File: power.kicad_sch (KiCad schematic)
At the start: 19 parts, among them IC1 RT8096AHGJ5, IC2 TLV61070A, Q1 SSM3J35AMFV

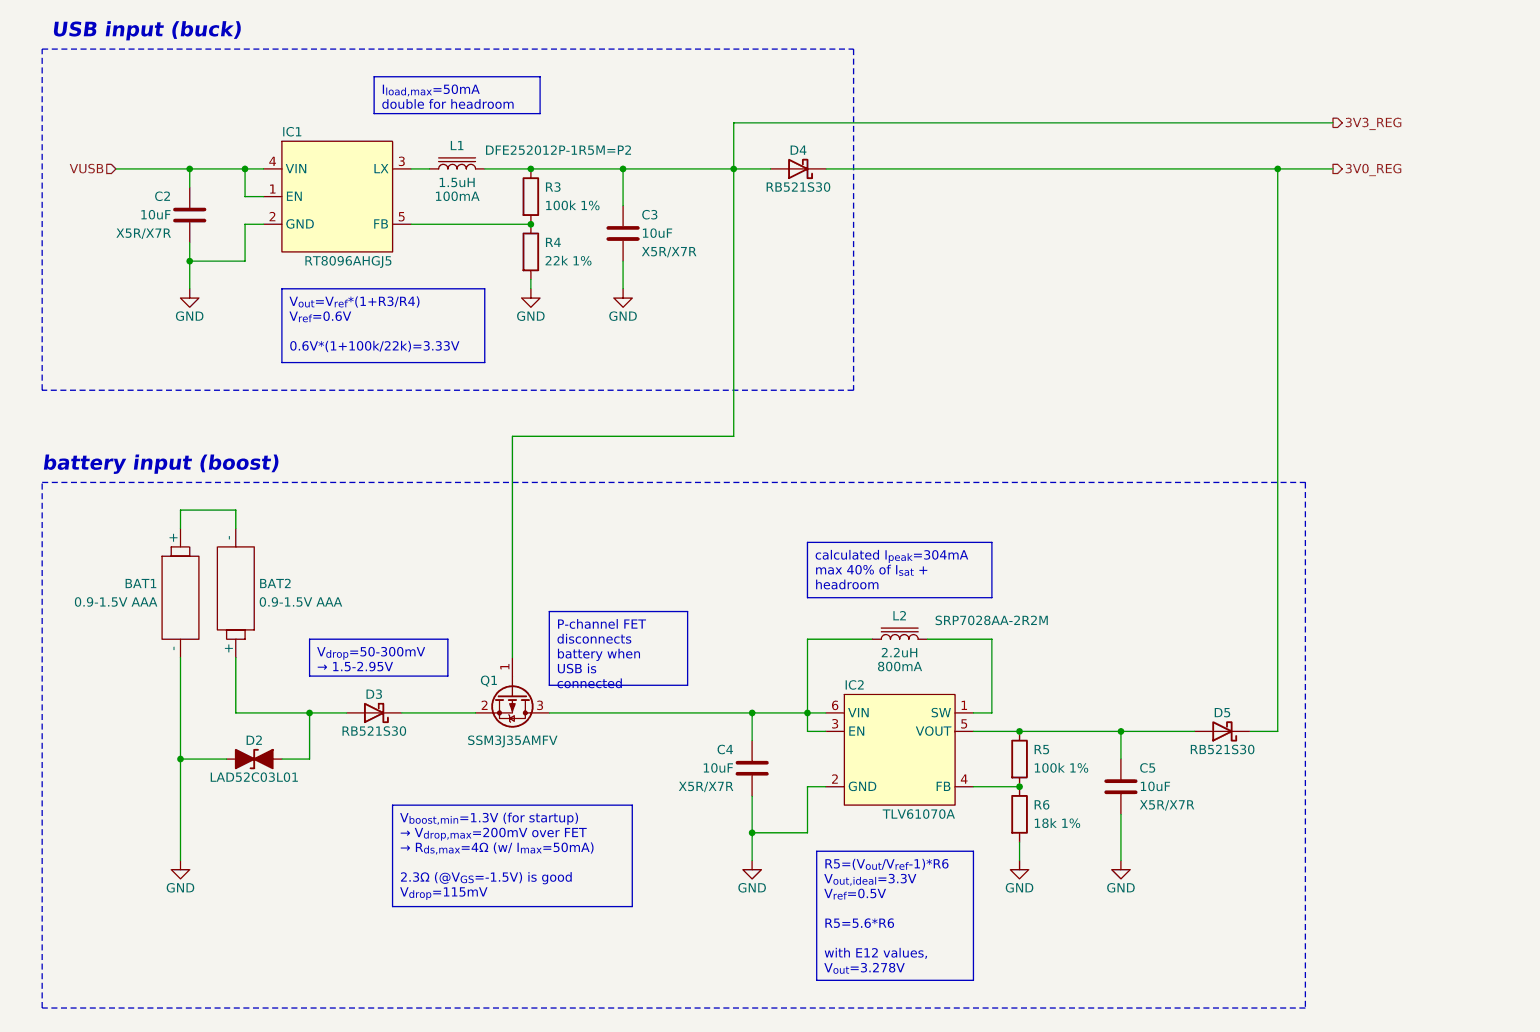
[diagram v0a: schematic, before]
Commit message: added testpoints
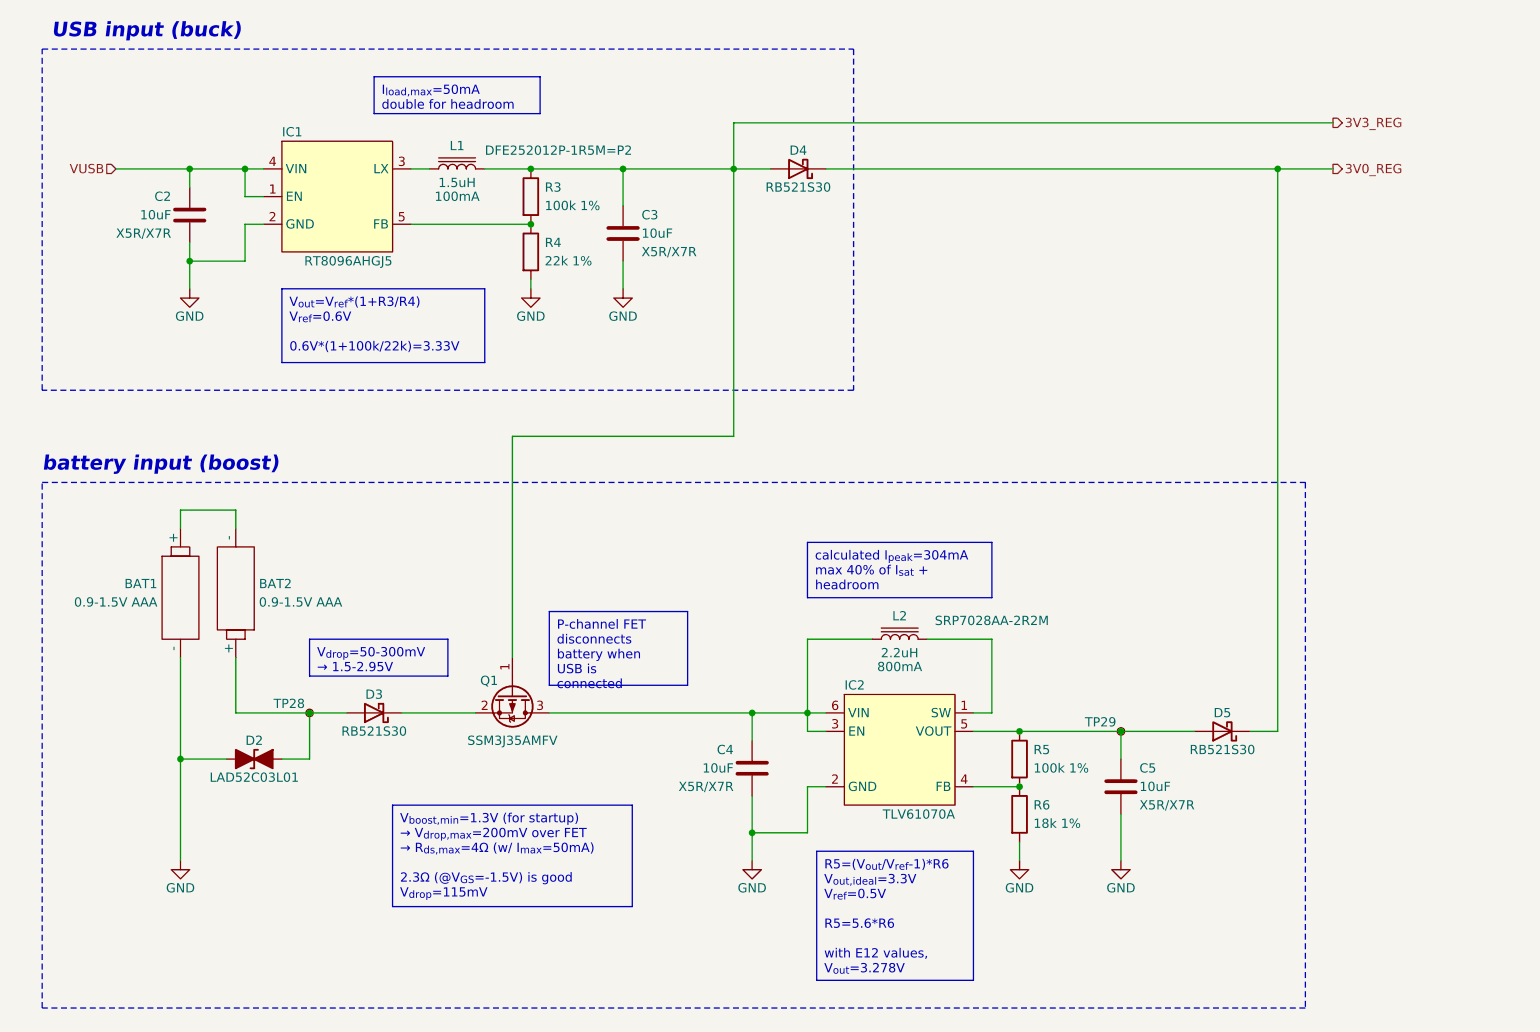
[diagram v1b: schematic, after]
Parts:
- added TP28, TP29: TestPoint_Small, TestPoint:TestPoint_Pad_D2.0mm, symbol Connector:TestPoint_Small
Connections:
- net at C5.1, D5.2 (A), IC2.5 (VOUT)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: now also TP29.1
- net at BAT2.1 (+), D2.2 (A2), D3.2 (A): now also TP28.1
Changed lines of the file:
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@@
     (stroke (width 0) (type default))
   )
-  (wire (pts (xy 233.68 41.91) (xy 151.13 41.91))
+  (wire (pts (xy 151.13 41.91) (xy 233.68 41.91))
     (stroke (width 0) (type default))
   )
@@
     (stroke (width 0) (type default))
   )
+  (wire (pts (xy 163.83 48.26) (xy 226.06 48.26))
+    (stroke (width 0) (type default))
+  )
   (wire (pts (xy 222.25 125.73) (xy 226.06 125.73))
     (stroke (width 0) (type default))
@@
   )
   (wire (pts (xy 161.29 113.03) (xy 161.29 123.19))
-    (stroke (width 0) (type default))
-  )
-  (wire (pts (xy 163.83 48.26) (xy 226.06 48.26))
     (stroke (width 0) (type default))
   )
@@
     )
   )
+  (symbol (lib_id "Connector:TestPoint_Small") (at 92.71 123.19 0) (mirror y) (unit 1)
+    (in_bom yes) (on_board yes) (dnp no)
+    (property "Reference" "TP28" (at 92.075 121.92 0)
+      (effects (font (size 1.27 1.27)) (justify left))
+    )
+    (property "Value" "TestPoint_Small" (at 91.44 124.46 0)
+      (effects (font (size 1.27 1.27)) (justify left) hide)
+    )
+    (property "Footprint" "TestPoint:TestPoint_Pad_D2.0mm" (at 87.63 123.19 0)
+      (effects (font (size 1.27 1.27)) hide)
+    )
+    (property "Datasheet" "~" (at 87.63 123.19 0)
+      (effects (font (size 1.27 1.27)) hide)
+    )
+    (pin "1")
+    (instances
+      (project "gkos_pebble"
+        (path "/ab6fff6e-44fa-4992-ab9d-8d9a7df4367d/cd56f630-7868-414d-908b-81d1bc89adae"
+          (reference "TP28") (unit 1)
+        )
+      )
+    )
+  )
   (symbol (lib_id "Device:R") (at 190.5 137.16 0) (unit 1)
     (in_bom yes) (on_board yes) (dnp no)
@@
   (symbol (lib_id "power:GND") (at 76.2 64.77 0) (unit 1)
     (in_bom yes) (on_board yes) (dnp no)
-    (property "Reference" "#PWR09" (at 76.2 71.12 0)
+    (property "Reference" "#PWR010" (at 76.2 71.12 0)
       (effects (font (size 1.27 1.27)) hide)
     )
@@
       (project "gkos_pebble"
         (path "/ab6fff6e-44fa-4992-ab9d-8d9a7df4367d/cd56f630-7868-414d-908b-81d1bc89adae"
-          (reference "#PWR09") (unit 1)
+          (reference "#PWR010") (unit 1)
         )
       )
@@
   (symbol (lib_id "power:GND") (at 74.93 143.51 0) (unit 1)
     (in_bom yes) (on_board yes) (dnp no)
-    (property "Reference" "#PWR010" (at 74.93 149.86 0)
+    (property "Reference" "#PWR09" (at 74.93 149.86 0)
       (effects (font (size 1.27 1.27)) hide)
     )
@@
       (project "gkos_pebble"
         (path "/ab6fff6e-44fa-4992-ab9d-8d9a7df4367d/cd56f630-7868-414d-908b-81d1bc89adae"
-          (reference "#PWR010") (unit 1)
+          (reference "#PWR09") (unit 1)
         )
       )
@@
         )
       )
+    )
+  )
+  (symbol (lib_id "Connector:TestPoint_Small") (at 204.47 125.73 0) (mirror y) (unit 1)
+    (in_bom yes) (on_board yes) (dnp no)
+    (property "Reference" "TP29" (at 203.835 124.46 0)
+      (effects (font (size 1.27 1.27)) (justify left))
+    )
+    (property "Value" "TestPoint_Small" (at 203.2 127 0)
+      (effects (font (size 1.27 1.27)) (justify left) hide)
+    )
+    (property "Footprint" "TestPoint:TestPoint_Pad_D2.0mm" (at 199.39 125.73 0)
+      (effects (font (size 1.27 1.27)) hide)
+    )
+    (property "Datasheet" "~" (at 199.39 125.73 0)
+      (effects (font (size 1.27 1.27)) hide)
+    )
+    (pin "1")
+    (instances
+      (project "gkos_pebble"
+        (path "/ab6fff6e-44fa-4992-ab9d-8d9a7df4367d/cd56f630-7868-414d-908b-81d1bc89adae"
+          (reference "TP29") (unit 1)
+        )
+      )

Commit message: test points
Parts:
- TP28: value TestPoint_Small -> VBAT
- TP29: value TestPoint_Small -> BOOS

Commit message: reannotate
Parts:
- renumbered TP28 to TP26, TP29 to TP27
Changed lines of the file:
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@@
   (symbol (lib_id "Connector:TestPoint_Small") (at 204.47 125.73 0) (mirror y) (unit 1)
     (in_bom yes) (on_board yes) (dnp no)
-    (property "Reference" "TP29" (at 203.835 124.46 0)
+    (property "Reference" "TP27" (at 203.835 124.46 0)
       (effects (font (size 1.27 1.27)) (justify left) hide)
     )
@@
       (project "gkos_pebble"
         (path "/ab6fff6e-44fa-4992-ab9d-8d9a7df4367d/cd56f630-7868-414d-908b-81d1bc89adae"
-          (reference "TP29") (unit 1)
+          (reference "TP27") (unit 1)
         )
       )
@@
   (symbol (lib_id "Connector:TestPoint_Small") (at 92.71 123.19 0) (mirror y) (unit 1)
     (in_bom yes) (on_board yes) (dnp no)
-    (property "Reference" "TP28" (at 92.075 121.92 0)
+    (property "Reference" "TP26" (at 92.075 121.92 0)
       (effects (font (size 1.27 1.27)) (justify left) hide)
     )
@@
       (project "gkos_pebble"
         (path "/ab6fff6e-44fa-4992-ab9d-8d9a7df4367d/cd56f630-7868-414d-908b-81d1bc89adae"
-          (reference "TP28") (unit 1)
-        )
-      )
+          (reference "TP26") (unit 1)
+        )
+      )

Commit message: in progress pcb
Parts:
- C2, C3, C4, C5: footprint Capacitor_SMD:C_0805_2012Metric -> Capacitor_SMD:C_0603_1608Metric
- R3, R4, R5, R6: footprint Resistor_SMD:R_0805_2012Metric -> Resistor_SMD:R_0603_1608Metric
- TP26, TP27: footprint TestPoint:TestPoint_Pad_D2.0mm -> TestPoint:TestPoint_Pad_D1.0mm
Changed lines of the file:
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@@
       (effects (font (size 1.27 1.27)) (justify right))
     )
-    (property "Footprint" "Capacitor_SMD:C_0805_2012Metric" (at 134.9248 60.96 0)
+    (property "Footprint" "Capacitor_SMD:C_0603_1608Metric" (at 134.9248 60.96 0)
       (effects (font (size 1.27 1.27)) hide)
     )
@@
       (effects (font (size 1.27 1.27)) (justify left))
     )
-    (property "Footprint" "Resistor_SMD:R_0805_2012Metric" (at 188.722 137.16 90)
+    (property "Footprint" "Resistor_SMD:R_0603_1608Metric" (at 188.722 137.16 90)
       (effects (font (size 1.27 1.27)) hide)
     )
@@
       (effects (font (size 1.27 1.27)) (justify left))
     )
-    (property "Footprint" "Resistor_SMD:R_0805_2012Metric" (at 121.412 52.07 90)
+    (property "Footprint" "Resistor_SMD:R_0603_1608Metric" (at 121.412 52.07 90)
       (effects (font (size 1.27 1.27)) hide)
     )
@@
       (effects (font (size 1.27 1.27)) (justify left))
     )
-    (property "Footprint" "TestPoint:TestPoint_Pad_D2.0mm" (at 199.39 125.73 0)
+    (property "Footprint" "TestPoint:TestPoint_Pad_D1.0mm" (at 199.39 125.73 0)
       (effects (font (size 1.27 1.27)) hide)
     )
@@
       (effects (font (size 1.27 1.27)) (justify right))
     )
-    (property "Footprint" "Capacitor_SMD:C_0805_2012Metric" (at 154.6352 134.62 0)
+    (property "Footprint" "Capacitor_SMD:C_0603_1608Metric" (at 154.6352 134.62 0)
       (effects (font (size 1.27 1.27)) hide)
     )
@@
       (effects (font (size 1.27 1.27)) (justify right))
     )
-    (property "Footprint" "Capacitor_SMD:C_0805_2012Metric" (at 77.1652 58.42 0)
+    (property "Footprint" "Capacitor_SMD:C_0603_1608Metric" (at 77.1652 58.42 0)
       (effects (font (size 1.27 1.27)) hide)
     )
@@
       (effects (font (size 1.27 1.27)) (justify left))
     )
-    (property "Footprint" "Resistor_SMD:R_0805_2012Metric" (at 121.412 59.69 90)
+    (property "Footprint" "Resistor_SMD:R_0603_1608Metric" (at 121.412 59.69 90)
       (effects (font (size 1.27 1.27)) hide)
     )
@@
       (effects (font (size 1.27 1.27)) (justify left))
     )
-    (property "Footprint" "Resistor_SMD:R_0805_2012Metric" (at 188.722 129.54 90)
+    (property "Footprint" "Resistor_SMD:R_0603_1608Metric" (at 188.722 129.54 90)
       (effects (font (size 1.27 1.27)) hide)
     )
@@
       (effects (font (size 1.27 1.27)) (justify right))
     )
-    (property "Footprint" "Capacitor_SMD:C_0805_2012Metric" (at 203.5048 137.16 0)
+    (property "Footprint" "Capacitor_SMD:C_0603_1608Metric" (at 203.5048 137.16 0)
       (effects (font (size 1.27 1.27)) hide)
     )
@@
       (effects (font (size 1.27 1.27)) (justify left))
     )
-    (property "Footprint" "TestPoint:TestPoint_Pad_D2.0mm" (at 87.63 123.19 0)
-      (effects (font (size 1.27 1.27)) hide)
-    )
+    (property "Footprint" "TestPoint:TestPoint_Pad_D1.0mm" (at 87.63 123.19 0)
+      (effects (font (size 1.27 1.27)) hide)
+    )

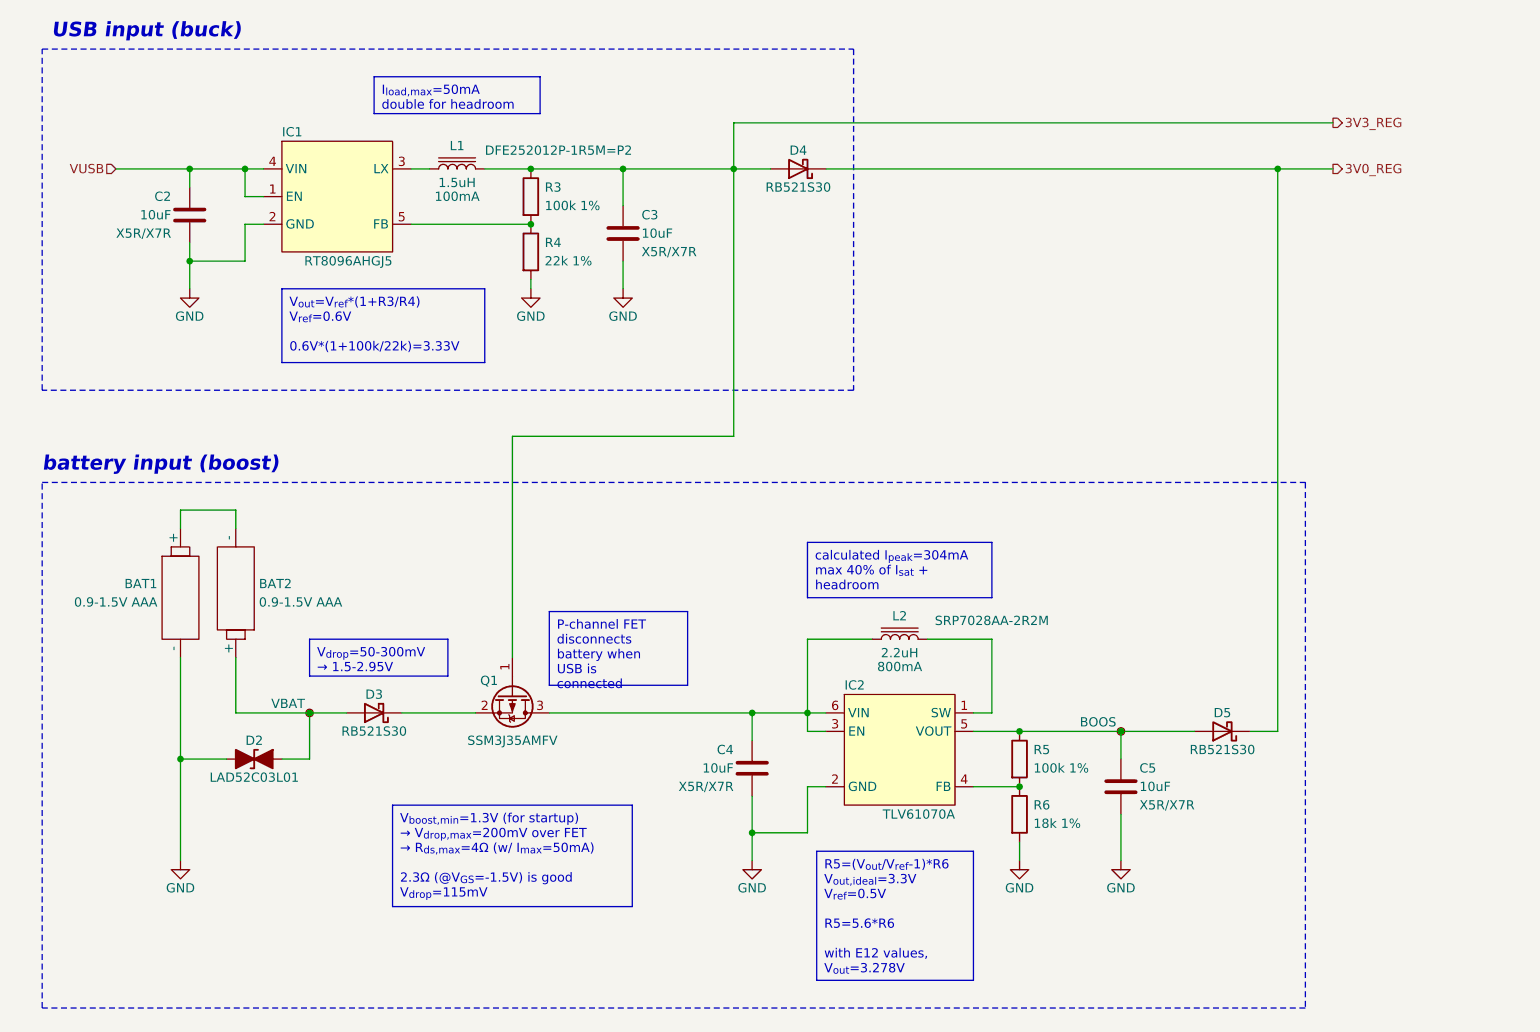
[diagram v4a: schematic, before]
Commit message: add second battery TVS
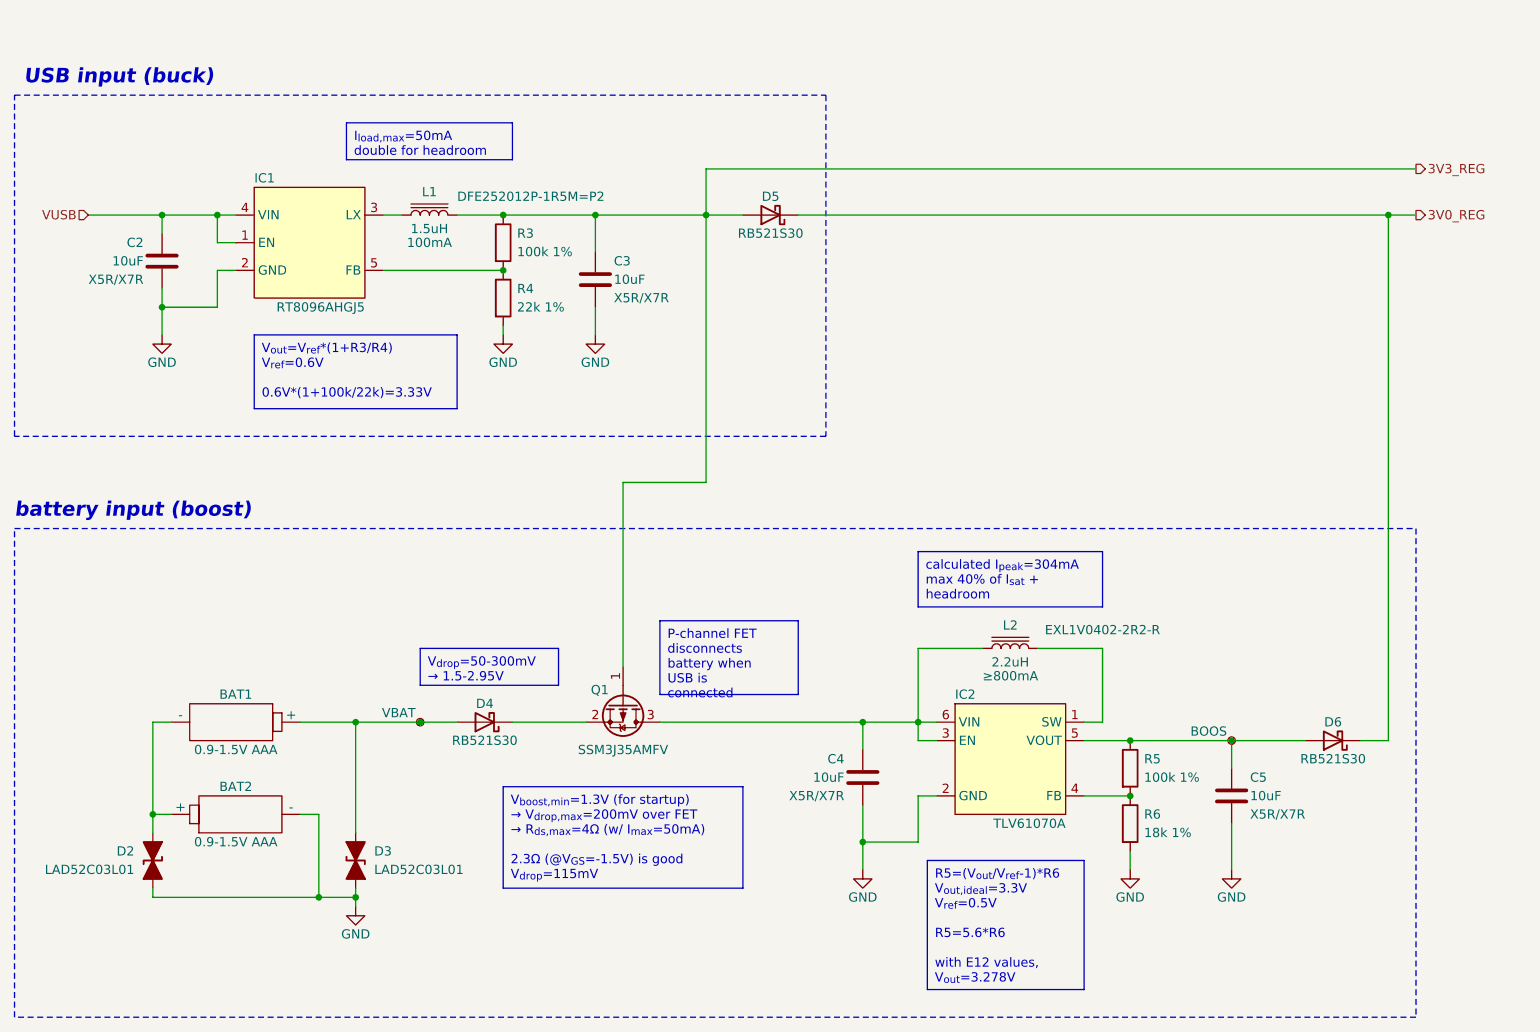
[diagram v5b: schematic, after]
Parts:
- added D2: LAD52C03L01, Diode_SMD:D_SOD-523, symbol Device:D_TVS_Filled
- L2: footprint Inductor_SMD:L_Bourns_SRP7028A_7.3x6.6mm -> footprints:EXL1V0402-2R2-R; Isat 800mA -> ≥800mA; Model SRP7028AA-2R2M -> EXL1V0402-2R2-R
- renumbered BAT2 to BAT1, BAT1 to BAT2, D2 to D3, D3 to D4, D4 to D5, D5 to D6
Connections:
- net GND: now also D2.1 (A1)
- net at BAT1.2 (-), BAT2.1 (+): now also D2.2 (A2)
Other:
- moved on the sheet: BAT1, BAT2, C2, C3, C4, C5, D3, D4, D5, D6, IC1, IC2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
